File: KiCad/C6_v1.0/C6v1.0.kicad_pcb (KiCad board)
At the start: 2 copper layers, 127 x 127 mm, 0 parts

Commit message: im scared
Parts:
- added 1.8LDO1: LP5907MFX-1.8, Package_TO_SOT_SMD:SOT-23-5, F.Cu at (49.9, 106.4)
- added 2.8LDO1: LP5907MFX-2.8, Package_TO_SOT_SMD:SOT-23-5, F.Cu at (49.9, 111.0)
- added BMS1: BQ29209DRBR, BQ29209:DRB8_1P6X2P4, F.Cu at (112.3, 51.1)
- added BUCKCONV1: TPS563200, Package_TO_SOT_SMD:SOT-23-6, F.Cu at (108.2, 63.5)
- added BatteryConnector1: B03B-XASK-1, B03B-XASK-1_JST:CONN_B03B-XASK-1_JST, F.Cu at (99.8, 47.2)
- added C1: 0.1u, Capacitor_SMD:C_0805_2012Metric, F.Cu at (-11.4, 34.5)
- added C10: 0.1u, Capacitor_SMD:C_0805_2012Metric, F.Cu at (-17.9, 96.6)
- added C11: 0.1u, Capacitor_SMD:C_0805_2012Metric, F.Cu at (-17.9, 99.6)
- added C12: 10u, Capacitor_SMD:C_0805_2012Metric, F.Cu at (-17.9, 102.6)
- added C13: 18p, Capacitor_SMD:C_0805_2012Metric, F.Cu at (-17.9, 105.6)
- added C14: 0.1u, Capacitor_SMD:C_0201_0603Metric_Pad0.64x0.40mm_HandSolder, F.Cu at (-2.70, 110.4)
- added C15: 18p, Capacitor_SMD:C_0805_2012Metric, F.Cu at (-17.9, 108.6)
- added C16: 0.1u, Capacitor_SMD:C_0805_2012Metric, F.Cu at (-17.9, 111.6)
- added C17: 18p, Capacitor_SMD:C_0805_2012Metric, F.Cu at (-17.9, 114.6)
- added C18: 10u, Capacitor_SMD:C_0805_2012Metric, F.Cu at (-13.5, 88.6)
- added C19: 0.1u, Capacitor_SMD:C_0805_2012Metric, F.Cu at (-13.5, 91.6)
- added C2: 1u, Capacitor_SMD:C_0805_2012Metric, F.Cu at (-11.4, 37.5)
- added C20: 0.1uF, Capacitor_SMD:C_1206_3216Metric, F.Cu at (112.0, 46.8)
- added C21: CL10B105KP8NNNC 1uf, Capacitor_SMD:C_1206_3216Metric, F.Cu at (38.9, 97.7)
- added C22: CL10B105KP8NNNC 1uf, Capacitor_SMD:C_1206_3216Metric, F.Cu at (38.9, 101.0)
- added C23: CL10B105KP8NNNC 1uf, Capacitor_SMD:C_1206_3216Metric, F.Cu at (38.9, 104.3)
- added C24: CL10B105KP8NNNC 1uf, Capacitor_SMD:C_1206_3216Metric, F.Cu at (38.9, 107.7)
- added C25: CL10B105KP8NNNC 1uf, Capacitor_SMD:C_1206_3216Metric, F.Cu at (38.9, 111.0)
- added C26: CL10B105KP8NNNC 1uf, Capacitor_SMD:C_1206_3216Metric, F.Cu at (38.9, 114.4)
- added C27: CL31B106KAHNNNE/10uf, CL31B106KAHNNNE:CAPC3216X180N, F.Cu at (108.8, 69.8)
- added C28: CL31B106KAHNNNE/10uf, CL31B106KAHNNNE:CAPC3216X180N, F.Cu at (108.8, 67.2)
- added C29: 08053C104KAT2A/0.1uf, Capacitor_SMD:C_1206_3216Metric, F.Cu at (104.0, 65.8)
- added C30: CL10A226MP8NUNE/22uf, Capacitor_SMD:C_1206_3216Metric, F.Cu at (118.5, 84.5)
- added C31: CL10A226MP8NUNE/22uf, Capacitor_SMD:C_1206_3216Metric, F.Cu at (114.8, 84.5)
- added C32: 2.2u, Capacitor_SMD:C_0805_2012Metric, F.Cu at (-11.4, 52.5)
- added C33: 2.2u, Capacitor_SMD:C_0805_2012Metric, F.Cu at (-11.4, 55.5)
- added C34: 0.1uF, Capacitor_SMD:C_1206_3216Metric, F.Cu at (106.2, 45.5)
- added C35: 10uF, Capacitor_SMD:C_1206_3216Metric, F.Cu at (95.0, 59.2)
- added C36: 0.33uF, Capacitor_SMD:C_1206_3216Metric, F.Cu at (106.2, 54.5)
- added C37: 0.1uF, Capacitor_SMD:C_1206_3216Metric, F.Cu at (95.0, 56.2)
- added C38: 0.1uF, Capacitor_SMD:C_1206_3216Metric, F.Cu at (110.5, 55.8)
- added C39: 0.1uF, Capacitor_SMD:C_1206_3216Metric, F.Cu at (126.0, 51.8)
- added C4: 0.1u, Capacitor_SMD:C_0805_2012Metric, F.Cu at (-11.4, 40.5)
- added C40: 0.1uF, Capacitor_SMD:C_1206_3216Metric, F.Cu at (119.8, 54.0)
- added C41: 0.1u, Capacitor_SMD:C_1206_3216Metric, F.Cu at (48.5, 39.2)
- added C5: 10u, Capacitor_SMD:C_0805_2012Metric, F.Cu at (-11.4, 43.5)
- added C6: 0.1u, Capacitor_SMD:C_0805_2012Metric, F.Cu at (-11.4, 46.5)
- added C7: 0.1u, Capacitor_SMD:C_0805_2012Metric, F.Cu at (29.0, 100.5)
- added C8: 0.1u, Capacitor_SMD:C_0805_2012Metric, F.Cu at (29.0, 103.5)
- added C9: 10p, Capacitor_SMD:C_0805_2012Metric, F.Cu at (-11.4, 49.5)
- added Current_Monitor1: INA219AxD, Package_SO:SOIC-8_3.9x4.9mm_P1.27mm, F.Cu at (101.5, 60.0)
- added DSUB1: ICD15S13E4GX00LF, ICD15S13E4GX00LF:AMPHENOL_ICD15S13E4GX00LF, F.Cu at (117.4, 39.5)
- added FB2: FerriteBead, Resistor_SMD:R_0805_2012Metric, F.Cu at (-7.00, 51.7)
- added FB3: FerriteBead, Inductor_SMD:L_0201_0603Metric_Pad0.64x0.40mm_HandSolder, F.Cu at (-2.70, 112.2)
- added H1: MountingHole, MountingHole:MountingHole_2.2mm_M2_Pad, F.Cu at (-25.1, 74.0)
- added H2: MountingHole, MountingHole:MountingHole_2.2mm_M2_Pad, F.Cu at (-25.1, 79.9)
- added H3: MountingHole, MountingHole:MountingHole_2.2mm_M2_Pad, F.Cu at (-25.1, 85.9)
- added H4: MountingHole, MountingHole:MountingHole_2.2mm_M2_Pad, F.Cu at (-25.1, 91.8)
- added J1: Conn_01x06_Pin, Connector_PinHeader_2.54mm:PinHeader_1x06_P2.54mm_Vertical, F.Cu at (-6.91, 35.3)
- added J2: Conn_01x06_Pin, Connector_PinHeader_2.54mm:PinHeader_1x06_P2.54mm_Vertical, F.Cu at (-2.32, 35.3)
- added J3: Conn_01x06, Connector_JST:JST_XA_B06B-XASK-1_1x06_P2.50mm_Vertical, F.Cu at (14.0, 74.2)
- added J4: 472192001, Connector_Card:microSD_HC_Molex_47219-2001, F.Cu at (-7.37, 79.0)
- added J5: Conn_01x05_Socket, Connector_PinSocket_2.00mm:PinSocket_1x05_P2.00mm_Vertical, F.Cu at (41.0, 74.2)
- added J6: Conn_01x06, Connector_JST:JST_XA_B06B-XASK-1_1x06_P2.50mm_Vertical, F.Cu at (37.0, 57.5)
- added J7: FH12-24S-0.5SH_55_, C6:CONN_FH12-22S-0.5SH55_HIR, F.Cu at (21.0, 93.0)
- added J8: Conn_01x02, Connector_PinHeader_2.54mm:PinHeader_1x02_P2.54mm_Vertical, F.Cu at (-25.8, 64.2)
- added J9: Conn_01x02, Connector_PinHeader_2.54mm:PinHeader_1x02_P2.54mm_Vertical, F.Cu at (-21.2, 64.2)
- added L1: SRN8040-3R3Y/3.3uH, Inductor_SMD:L_Bourns-SRN8040_8x8.15mm, F.Cu at (116.2, 76.5)
- added LED1: LTST-C190KRKT, LTST_C190KRKT:LED_LTST-C190_LTO, F.Cu at (103.0, 72.9)
- added LED2: LTST-C190KRKT, LTST_C190KRKT:LED_LTST-C190_LTO, F.Cu at (53.7, 97.2)
- added LED3: LTST-C190KRKT, LTST_C190KRKT:LED_LTST-C190_LTO, F.Cu at (53.7, 99.7)
- added LED4: LTST-C190KRKT, LTST_C190KRKT:LED_LTST-C190_LTO, F.Cu at (53.7, 102.2)
- added Q1: 2N2219, Package_TO_SOT_THT:TO-39-3, F.Cu at (117.4, 61.5)
- added Q2: NTR4501NT1G, NTR4501NT1G:SOT95P237X111-3N, F.Cu at (126.4, 56.4)
- added Q3: PMOS, NTR4501NT1G:SOT95P237X111-3N, F.Cu at (119.1, 49.2)
- added R1: R22, Resistor_SMD:R_0805_2012Metric, F.Cu at (29.0, 106.5)
- added R10: R22, Resistor_SMD:R_0805_2012Metric, F.Cu at (-7.00, 60.6)
- added R11: R22, Resistor_SMD:R_0805_2012Metric, F.Cu at (-7.00, 63.5)
- added R12: R22, Resistor_SMD:R_0805_2012Metric, F.Cu at (-2.59, 51.7)
- added R13: R22, Resistor_SMD:R_0805_2012Metric, F.Cu at (-2.59, 54.7)
- added R14: R22, Resistor_SMD:R_0805_2012Metric, F.Cu at (-2.59, 57.6)
- added R15: R22, Resistor_SMD:R_0805_2012Metric, F.Cu at (-2.59, 60.6)
- added R16: R22, Resistor_SMD:R_0805_2012Metric, F.Cu at (-2.59, 63.5)
- added R17: YC164-JR-0733RL, C6:RES_YC124_2X1_YAG-L, F.Cu at (-9.76, 113.6)
- added R18: YC164-JR-0733RL, C6:RES_YC124_2X1_YAG-L, F.Cu at (-6.71, 113.6)
- added R19: R33, Resistor_SMD:R_0402_1005Metric_Pad0.72x0.64mm_HandSolder, F.Cu at (0.34, 110.5)
- added R2: R22, Resistor_SMD:R_0805_2012Metric, F.Cu at (29.0, 109.5)
- added R20: R0, Resistor_SMD:R_0805_2012Metric, F.Cu at (-13.5, 105.8)
- added R21: R51, Resistor_SMD:R_0805_2012Metric, F.Cu at (-13.5, 108.8)
- added R22: 10k, Resistor_SMD:R_0805_2012Metric, F.Cu at (-13.5, 111.8)
- added R23: 10k, Resistor_SMD:R_0805_2012Metric, F.Cu at (1.82, 51.7)
- added R24: 10k, Resistor_SMD:R_0805_2012Metric, F.Cu at (1.82, 54.7)
- added R25: 10k, Resistor_SMD:R_0805_2012Metric, F.Cu at (-17.9, 72.5)
- added R26: 10k, Resistor_SMD:R_0805_2012Metric, F.Cu at (-17.9, 75.4)
- added R27: 10k, Resistor_SMD:R_0805_2012Metric, F.Cu at (-17.9, 78.4)
- added R28: 10k, Resistor_SMD:R_0805_2012Metric, F.Cu at (-17.9, 81.3)
- added R29: 10k, Resistor_SMD:R_0805_2012Metric, F.Cu at (-17.9, 84.3)
- added R3: 200k, Resistor_SMD:R_0805_2012Metric, F.Cu at (12.6, 100.5)
- added R30: R22, Resistor_SMD:R_0805_2012Metric, F.Cu at (-17.9, 87.2)
- added R31: 68k 1%, Resistor_SMD:R_0603_1608Metric_Pad0.98x0.95mm_HandSolder, F.Cu at (60.0, 36.2)
- added R32: 33k 1%, Resistor_SMD:R_0603_1608Metric_Pad0.98x0.95mm_HandSolder, F.Cu at (60.0, 38.2)
- added R33: 51k, Resistor_SMD:R_1206_3216Metric, F.Cu at (116.8, 54.0)
- added R34: 160, Resistor_SMD:R_1206_3216Metric, F.Cu at (116.0, 48.5)
- added R35: 260, Resistor_SMD:R_1206_3216Metric, F.Cu at (106.2, 48.5)
- added R36: 100, Resistor_SMD:R_1206_3216Metric, F.Cu at (106.2, 51.5)
- added R37: 2m, Resistor_SMD:R_1206_3216Metric, F.Cu at (107.5, 58.5)
- added R38: 330k, Resistor_SMD:R_1206_3216Metric, F.Cu at (122.8, 49.0)
- added R39: 100, Resistor_SMD:R_1206_3216Metric, F.Cu at (113.6, 55.7)
- added R4: 2.2k, Resistor_SMD:R_0805_2012Metric, F.Cu at (12.6, 103.4)
- added R40: 1k, Resistor_SMD:R_1206_3216Metric, F.Cu at (130.0, 56.0)
- added R41: 470k, Resistor_SMD:R_1206_3216Metric, F.Cu at (122.8, 54.0)
- added R42: RC0805FR-07150RL, Resistor_SMD:R_1206_3216Metric, F.Cu at (44.5, 105.7)
- added R43: ERJ-2RKF1000X, Resistor_SMD:R_1206_3216Metric, F.Cu at (44.5, 109.0)
- added R44: RC0805FR-07150RL, Resistor_SMD:R_1206_3216Metric, F.Cu at (44.5, 112.3)
- added R45: 10k, Resistor_SMD:R_1206_3216Metric, F.Cu at (95.0, 62.0)
- added R46: RC1206FR-07249RL/220ohm, Resistor_SMD:R_1206_3216Metric, F.Cu at (101.5, 77.2)
- added R47: RC0201FR-0756K2L/56.2K ohm, Resistor_SMD:R_1206_3216Metric, F.Cu at (104.5, 77.2)
- added R48: RC0201FR-0710KL/10kohm, Resistor_SMD:R_1206_3216Metric, F.Cu at (108.8, 72.7)
- added R49: 10k, Resistor_SMD:R_0805_2012Metric, F.Cu at (1.82, 57.6)
- added R5: 2.2k, Resistor_SMD:R_0805_2012Metric, F.Cu at (12.6, 106.4)
- added R50: 10k, Resistor_SMD:R_0805_2012Metric, F.Cu at (1.82, 60.6)
- added R6: 2.2k, Resistor_SMD:R_0805_2012Metric, F.Cu at (12.6, 109.3)
- added R7: 2.2k, Resistor_SMD:R_0805_2012Metric, F.Cu at (12.6, 112.3)
- added R8: 220, Resistor_SMD:R_0805_2012Metric, F.Cu at (-7.00, 55.0)
- added R9: 220, Resistor_SMD:R_0805_2012Metric, F.Cu at (-7.00, 57.6)
- added SW1: SLW-1277545-3A-RA-N-D, SLW_1277545_3A_RA_N_D:SW_SLW-1277545-3A-RA-N-D, F.Cu at (97.0, 70.8)
- added U1: STM32H562RITx, Package_QFP:LQFP-64_10x10mm_P0.5mm, F.Cu at (-20.9, 40.2)
- added U10: REF35330QDBVR, Package_TO_SOT_SMD:SOT-23-6, F.Cu at (2.55, 41.9)
- added U2: STM32H7A3RITx, Package_QFP:LQFP-64_10x10mm_P0.5mm, F.Cu at (-20.9, 54.6)
- added U3: PCA9306, Package_SON:X2SON-8_1.4x1mm_P0.35mm, F.Cu at (16.3, 100.5)
- added U4: SN74CB3T3384PWR, C6:PW24-L, F.Cu at (-11.2, 99.7)
- added U5: SN74CB3T3384PWR, C6:PW24-L, F.Cu at (0.75, 94.8)
- added U6: ADV7280AWBCPZ, C6:CP-32-12_ADI-L, F.Cu at (-7.86, 108.1)
- added U7: MAX3490xSA, Package_SO:SOIC-8_3.9x4.9mm_P1.27mm, F.Cu at (4.20, 36.3)
- added U8: TLV1117LV33DCYR, TLV1117LV33DCYR:VREG_TLV1117LV33DCYR, F.Cu at (47.0, 100.0)
- added U9: OPA340NA, Package_TO_SOT_SMD:SOT-23-5, F.Cu at (54.1, 37.5)
- added Y1: SIT5000AICGE-33E0-25.000000X, Oscillator:Oscillator_SMD_SiT_PQFN-4Pin_5.0x3.2mm, F.Cu at (23.2, 101.7)
- added Y2: SIT5000AICGE-33E0-25.000000X, Oscillator:Oscillator_SMD_SiT_PQFN-4Pin_5.0x3.2mm, F.Cu at (23.2, 107.1)
- added Y3: ABM8AIG-28.63636MHZ, C6:XTAL_ABM8AIG-28.63636MHZ-12-2Z-T3, F.Cu at (-1.25, 107.0)
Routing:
- net /5V: track 0.00 -> 34.0 mm, vias 0 -> 3
- net Net-(BUCKCONV1-VFB): track 0.00 -> 26.3 mm, vias 0 -> 3
- net Net-(R45-Pad2): track 0.00 -> 14.2 mm
- net Net-(Q1-C): track 0.00 -> 12.0 mm
- net Net-(BMS1-VC1): track 0.00 -> 10.4 mm
- net Net-(Q1-B): track 0.00 -> 9.92 mm
- net GND: track 0.00 -> 9.78 mm, vias 0 -> 15
- net Net-(BatteryConnector1-Pad2): track 0.00 -> 8.50 mm
- net Net-(BMS1-VDD): track 0.00 -> 7.82 mm
- net Net-(BMS1-VC2): track 0.00 -> 7.41 mm
- net /8V4: track 0.00 -> 6.20 mm
- net /Power/Buck Converter/buck-vbst_cap: track 0.00 -> 5.94 mm, vias 0 -> 10
- net Net-(BUCKCONV1-VBST): track 0.00 -> 4.86 mm
- net /Power/8V4_Evil: track 0.00 -> 4.69 mm, vias 0 -> 15
- net Net-(Q2-Pad3): track 0.00 -> 4.38 mm
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- added copper zone on F.Cu, net +5V
- added copper zone on In2.Cu, net +5V
- added copper zone on F.Cu, net /8V4
- added copper zone on F.Cu, net /Power/8V4_Evil
- added copper zone on In2.Cu, net /Power/8V4_Evil
- added copper zone on F.Cu, net /Power/Buck Converter/buck-vbst_cap
- added copper zone on In2.Cu, net /Power/Buck Converter/buck-vbst_cap
- added copper zone on F.Cu, net /Power/VOUT
- added copper zone on In2.Cu, net /Power/VOUT
- added copper zone on F.Cu, net /Power/bruh
- added copper zone on F.Cu, net GND
- added copper zone on In1.Cu, net GND
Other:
- copper layers 2 -> 4

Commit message: DCMI1-Me0
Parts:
- added J10: Conn_01x03, Connector_JST:JST_XA_S03B-XASK-1_1x03_P2.50mm_Horizontal, F.Cu at (66.5, 85.6)
- added J11: Conn_01x06, Connector_JST:JST_XA_S06B-XASK-1_1x06_P2.50mm_Horizontal, F.Cu at (66.5, 71.0)
- added J12: Conn_02x10_Odd_Even, Connector_PinHeader_2.54mm:PinHeader_2x10_P2.54mm_Vertical, F.Cu at (58.2, 68.8)
- C1, C10, C11, C12, C13, C15, C16, C17, C18, C19, C2, C32, C33, C4, C5, C6, C7, C8, C9: footprint Capacitor_SMD:C_0805_2012Metric -> Capacitor_SMD:C_0402_1005Metric_Pad0.74x0.62mm_HandSolder
- C14: footprint Capacitor_SMD:C_0201_0603Metric_Pad0.64x0.40mm_HandSolder -> Capacitor_SMD:C_0402_1005Metric_Pad0.74x0.62mm_HandSolder
- J3, J6: footprint Connector_JST:JST_XA_B06B-XASK-1_1x06_P2.50mm_Vertical -> Connector_JST:JST_XA_S06B-XASK-1_1x06_P2.50mm_Horizontal
- R1, R10, R11, R12, R13, R14, R15, R16, R2, R20, R21, R22, R23, R24, R25, R26, R27, R28, R29, R3, R30, R4, R49, R5, R50, R6, R7, R8, R9: footprint Resistor_SMD:R_0805_2012Metric -> Resistor_SMD:R_0402_1005Metric_Pad0.72x0.64mm_HandSolder
- moved C12 191.7 mm to (172.4, 80.1), turned to 90 degrees
- moved C13 191.6 mm to (172.4, 83.3)
- moved C15 191.3 mm to (172.3, 88.5), turned to 180 degrees
- moved C16 190.6 mm to (169.6, 77.7), turned to 180 degrees
- moved C17 189.5 mm to (167.8, 76.9), turned to -90 degrees
- moved R21 186.6 mm to (170.2, 76.0), turned to -90 degrees
- moved R20 183.9 mm to (169.3, 85.2), turned to 135 degrees
- moved U4 182.2 mm to (170.9, 105.3)
- moved R22 181.9 mm to (165.1, 76.9), turned to 180 degrees
- moved FB3 180.3 mm to (174.8, 80.8), turned to 180 degrees
- moved U2 179.5 mm to (151.0, 106.4), turned to 135 degrees
- moved C14 176.8 mm to (171.4, 80.1), turned to 90 degrees
- moved U6 175.2 mm to (165.5, 82.5), turned to 45 degrees
- moved Y3 174.9 mm to (172.3, 85.9), turned to 180 degrees
- moved J7 167.0 mm to (187.3, 108.3), turned to 90 degrees
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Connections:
- net /STM32/PPS renamed /PPS
- R45 pad 2: Net-(R45-Pad2) -> Net-(BUCKCONV1-EN)
- U1 pad 20: unconnected-(U1-PA4-Pad20) -> /HALL_C
- U1 pad 22: unconnected-(U1-PA6-Pad22) -> /HALL_B
- U1 pad 23: unconnected-(U1-PA7-Pad23) -> /HALL_A
- U1 pad 27: unconnected-(U1-PB1-Pad27) -> /ESC_PWM
- U1 pad 57: unconnected-(U1-PB5-Pad57) -> /ESC_TLM
- U4 pad 10: /CAM_D4 -> unconnected-(U4-1B5-Pad10)
- U4 pad 11: /OV_D4 -> GND
- U4 pad 14: /OV_D5 -> /OV_D7
- U4 pad 15: /CAM_D5 -> /CAM_D7
- U4 pad 18: /OV_D7 -> /OV_PCLK
- U4 pad 19: /CAM_D7 -> /CAM_PCLK
- U4 pad 2: /CAM_D0 -> /CAM_D2
- U4 pad 20: /CAM_PCLK -> /CAM_D0
- U4 pad 21: /OV_PCLK -> /OV_D0
- U4 pad 22: GND -> /OV_D1
- U4 pad 23: unconnected-(U4-2B5-Pad23) -> /CAM_D1
- U4 pad 3: /OV_D0 -> /OV_D2
- U4 pad 4: /OV_D1 -> /OV_D3
- U4 pad 5: /CAM_D1 -> /CAM_D3
- U4 pad 6: /CAM_D2 -> /CAM_D4
- U4 pad 7: /OV_D2 -> /OV_D4
- U4 pad 8: /OV_D3 -> /OV_D5
- U4 pad 9: /CAM_D3 -> /CAM_D5
- U6 pad 21: /1V8 -> /CameraManagement/1V8*
- U7 pad 5: /STM32/RX- -> /RS422_RX-
- U7 pad 6: /STM32/RX+ -> /RS422_RX+
- U7 pad 7: /STM32/TX- -> /RS422_TX-
- U7 pad 8: /STM32/TX+ -> /RS422_TX+
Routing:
- net /CameraManagement/1V8*: track 0.00 -> 30.8 mm, vias 0 -> 5
- net /OV_D7: track 0.00 -> 19.5 mm
- net /OV_D0: track 0.00 -> 19.4 mm
- net /OV_D6: track 0.00 -> 19.4 mm
- net /OV_PCLK: track 0.00 -> 19.4 mm
- net /OV_D1: track 0.00 -> 19.4 mm
- net /OV_D4: track 0.00 -> 16.5 mm, vias 0 -> 2
- net /OV_D2: track 0.00 -> 16.5 mm, vias 0 -> 2
- net /OV_D3: track 0.00 -> 16.4 mm, vias 0 -> 2
- net /OV_D5: track 0.00 -> 16.4 mm, vias 0 -> 2
- net /CameraManagement/SPLIT_PCLK: track 0.00 -> 16.3 mm
- net /NTSC: track 0.00 -> 14.8 mm
- net /CameraManagement/SPLIT_D7: track 0.00 -> 14.3 mm
- net /CameraManagement/SPLIT_D0: track 0.00 -> 12.5 mm
- net /CameraManagement/SPLIT_D6: track 0.00 -> 12.2 mm
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
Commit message: john d tickle
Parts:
- removed SW1: SLW-1277545-3A-RA-N-D, SLW_1277545_3A_RA_N_D:SW_SLW-1277545-3A-RA-N-D
- moved BatteryConnector1 14.9 mm to (103.5, 32.8), turned to 0 degrees
- moved C40 13.0 mm to (132.8, 54.5)
- moved DSUB1 13.0 mm to (130.4, 40.0)
- moved Q1 13.0 mm to (130.4, 62.0)
- moved R33 13.0 mm to (129.8, 54.5)
- moved R39 13.0 mm to (126.6, 56.1)
- moved BMS1 13.0 mm to (125.3, 51.6)
- moved BUCKCONV1 13.0 mm to (121.2, 64.0)
- moved C20 13.0 mm to (125.0, 47.2)
- moved C27 13.0 mm to (121.7, 70.2)
- moved C28 13.0 mm to (121.7, 67.7)
- moved C29 13.0 mm to (117.0, 66.3)
- moved C30 13.0 mm to (131.5, 85.0)
- moved C31 13.0 mm to (127.7, 85.0)
- moved C34 13.0 mm to (119.2, 46.0)
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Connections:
- DSUB1 pad S1: unconnected-(DSUB1-SHIELD-PadS1) -> GND
- DSUB1 pad S2: unconnected-(DSUB1-SHIELD__1-PadS2) -> GND
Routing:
- net Net-(R45-Pad2): track 14.2 -> 0.00 mm
- net GND: vias 15 -> 17

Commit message: sneaky commit
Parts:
- removed BatteryConnector1: B03B-XASK-1, B03B-XASK-1_JST:CONN_B03B-XASK-1_JST
- added J13: S02B-XASS-1LFSN, idk:CONN2_S02B-XASS_295x496_JST, F.Cu at (190.0, 40.0)
- added J14: Conn_01x03, Connector_JST:JST_XA_S03B-XASK-1_1x03_P2.50mm_Horizontal, F.Cu at (107.5, 42.9)
- moved J3 139.3 mm to (136.2, 141.0)
- moved J12 43.4 mm to (100.1, 80.2)
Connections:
- R45 pad 1: /8V4 -> Net-(BUCKCONV1-EN)
- R45 pad 2: Net-(BUCKCONV1-EN) -> GND
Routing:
- net Net-(BUCKCONV1-EN): track 0.00 -> 6.20 mm
- net /8V4: track 6.20 -> 0.00 mm

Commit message: finaly
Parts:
- removed C11: 0.1u, Capacitor_SMD:C_0402_1005Metric_Pad0.74x0.62mm_HandSolder
- removed DSUB1: ICD15S13E4GX00LF, ICD15S13E4GX00LF:AMPHENOL_ICD15S13E4GX00LF
- removed J13: S02B-XASS-1LFSN, idk:CONN2_S02B-XASS_295x496_JST
- removed R10, R11, R12, R13: R22, Resistor_SMD:R_0402_1005Metric_Pad0.72x0.64mm_HandSolder
- removed R19: R33, Resistor_SMD:R_0402_1005Metric_Pad0.72x0.64mm_HandSolder
- removed R23: 10k, Resistor_SMD:R_0402_1005Metric_Pad0.72x0.64mm_HandSolder
- removed R45: 10k, Resistor_SMD:R_1206_3216Metric
- removed U4, U5: SN74CB3T3384PWR, C6:PW24-L
- added C3: 2.2u, Capacitor_SMD:C_0402_1005Metric_Pad0.74x0.62mm_HandSolder, F.Cu at (114.2, 108.7)
- added J15: Conn_02x03_Odd_Even, C6:CONN_SD-44764-001_06_MOL, F.Cu at (195.6, 33.2)
- added R51: R33, Resistor_SMD:R_0402_1005Metric_Pad0.72x0.64mm_HandSolder, B.Cu at (180.9, 103.0)
- added R52: R33, Resistor_SMD:R_0402_1005Metric_Pad0.72x0.64mm_HandSolder, B.Cu at (180.9, 102.0)
- added R53: R33, Resistor_SMD:R_0402_1005Metric_Pad0.72x0.64mm_HandSolder, B.Cu at (180.9, 101.0)
- added R54: R33, Resistor_SMD:R_0402_1005Metric_Pad0.72x0.64mm_HandSolder, B.Cu at (180.9, 99.9)
- added R55: R33, Resistor_SMD:R_0402_1005Metric_Pad0.72x0.64mm_HandSolder, B.Cu at (180.9, 98.9)
- added R56: R33, Resistor_SMD:R_0402_1005Metric_Pad0.72x0.64mm_HandSolder, B.Cu at (180.9, 97.9)
- added R57: R33, Resistor_SMD:R_0402_1005Metric_Pad0.72x0.64mm_HandSolder, B.Cu at (180.9, 96.9)
- added R58: R33, Resistor_SMD:R_0402_1005Metric_Pad0.72x0.64mm_HandSolder, B.Cu at (180.9, 95.9)
- added R59: R33, Resistor_SMD:R_0402_1005Metric_Pad0.72x0.64mm_HandSolder, B.Cu at (180.9, 94.9)
- added R60: R33, Resistor_SMD:R_0402_1005Metric_Pad0.72x0.64mm_HandSolder, B.Cu at (180.9, 93.9)
- added R61: R33, Resistor_SMD:R_0402_1005Metric_Pad0.72x0.64mm_HandSolder, B.Cu at (180.9, 92.8)
- added R62: YC164-JR-0733RL, C6:RES_YC124_2X1_YAG-L, F.Cu at (146.1, 100.3)
- added U11: SN74CBTLV16292VR, C6:DGV56-L, F.Cu at (151.5, 96.6)
- C10: value 0.1u -> 2.2u
- FB3: footprint Inductor_SMD:L_0201_0603Metric_Pad0.64x0.40mm_HandSolder -> Inductor_SMD:L_0805_2012Metric_Pad1.15x1.40mm_HandSolder
- J7: moved to B.Cu
- U3: footprint Package_SON:X2SON-8_1.4x1mm_P0.35mm -> Package_SO:SSOP-8_2.95x2.8mm_P0.65mm
- moved H4 226.4 mm to (198.1, 129.7)
- moved U1 226.2 mm to (139.7, 121.3), turned to -135 degrees
- moved H3 225.6 mm to (198.1, 53.5)
- moved R25 206.3 mm to (175.0, 145.4)
- moved R27 206.3 mm to (175.0, 151.3)
- moved R26 205.6 mm to (175.0, 146.6)
- moved R28 205.6 mm to (175.0, 152.4)
- moved R29 203.9 mm to (175.0, 150.1)
- moved C18 197.6 mm to (175.0, 147.7)
- moved C19 197.1 mm to (175.0, 149.0)
- moved C9 190.9 mm to (176.3, 84.6), turned to -90 degrees
- moved J9 185.7 mm to (153.7, 126.5), turned to -90 degrees
- moved R9 185.6 mm to (176.9, 82.9)
- moved J4 185.3 mm to (164.7, 147.7)
- moved R30 179.1 mm to (154.9, 134.1), turned to 135 degrees
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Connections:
- net /DCMI_RST renamed /OV_RST
- net /OV_OE renamed /CAM_S
- 1.8LDO1 pad 1: +2.8V -> /2V8
- 1.8LDO1 pad 3: +2.8V -> /2V8
- 1.8LDO1 pad 5: 1.8V -> /1V8
- 2.8LDO1 pad 1: +3.3V -> /3V3
- 2.8LDO1 pad 3: +3.3V -> /3V3
- 2.8LDO1 pad 5: +2.8V -> /2V8
- BMS1 pad 9: unconnected-(BMS1-EPAD-Pad9) -> GND
- BUCKCONV1 pad 5: Net-(BUCKCONV1-EN) -> /8V4
- C10 pad 1: /3V3 -> Net-(C10-Pad1)
- C21 pad 2: +5V -> /5V
- C22 pad 2: +3.3V -> /3V3
- C23 pad 2: +2.8V -> /2V8
- C24 pad 2: 1.8V -> /1V8
- C25 pad 2: +2.8V -> /2V8
- C26 pad 2: +3.3V -> /3V3
- C30 pad 2: +5V -> /5V
- C31 pad 2: +5V -> /5V
- J11 pad 6: /IO_Connections/3V3 -> /3V3
- J12 pad 3: /IO_Connections/3V3 -> /3V3
- J12 pad 4: /IO_Connections/3V3 -> /3V3
- J7 pad 12: /OV_D7 -> /IO_Connections/D7
- J7 pad 14: /OV_D6 -> /IO_Connections/D6
- J7 pad 16: /OV_D5 -> /IO_Connections/D5
- J7 pad 17: /OV_PCLK -> /IO_Connections/PCLK
- J7 pad 18: /OV_D4 -> /IO_Connections/D4
- J7 pad 19: /OV_D0 -> /IO_Connections/D0
- J7 pad 20: /OV_D3 -> /IO_Connections/D3
- J7 pad 21: /OV_D1 -> /IO_Connections/D1
- J7 pad 22: /OV_D2 -> /IO_Connections/D2
- J7 pad 7: /CAM_VSYNC -> /IO_Connections/VSYNC
- J7 pad 8: /DCMI_PWDN -> /OV_PWDN
- J7 pad 9: /CAM_HSYNC -> /IO_Connections/HSYNC
- L1 pad 1: +5V -> /5V
- R17 pad 1: /CAM_D0 -> /CAM_PWDN*
- R17 pad 2: /CAM_D1 -> /CAM_D7*
- R17 pad 3: /CAM_D2 -> /CAM_D6*
- R17 pad 4: /CAM_D3 -> /CAM_VSYNC*
- R17 pad 5: /CAM_D3 -> /CameraManagement/CAM_VSYNC
- R17 pad 6: /CAM_D2 -> /CameraManagement/CAM_D6
- R17 pad 7: /CAM_D1 -> /CameraManagement/CAM_D7
- R17 pad 8: /CAM_D0 -> /CameraManagement/CAM_PDWN
- R18 pad 1: /CAM_D4 -> /CAM_D5*
- R18 pad 2: /CAM_D5 -> /CAM_D4*
- R18 pad 3: /CAM_D6 -> /CAM_HSYNC*
- R18 pad 4: /CAM_D7 -> /CAM_PCLK*
- R18 pad 5: /CAM_D7 -> /CameraManagement/CAM_PCLK
- R18 pad 6: /CAM_D6 -> /CameraManagement/CAM_HSYNC
- R18 pad 7: /CAM_D5 -> /CameraManagement/CAM_D4
- R18 pad 8: /CAM_D4 -> /CameraManagement/CAM_D5
- R42 pad 1: +2.8V -> /2V8
- R43 pad 1: 1.8V -> /1V8
- R44 pad 1: +3.3V -> /3V3
- R46 pad 2: +5V -> /5V
- R47 pad 2: +5V -> /5V
- U1 pad 29: /STM32/SPI_SCK* -> /STM32/SPI_SCK
- U1 pad 30: Net-(C32-Pad1) -> Net-(C10-Pad1)
- U1 pad 33: /STM32/SPI_NSS* -> /STM32/SPI_NSS
- U1 pad 35: /STM32/SPI_MISO* -> /STM32/SPI_MISO
- U1 pad 36: /STM32/SPI_MOSI* -> /STM32/SPI_MOSI
- U2 pad 10: /SPLIT_OE -> unconnected-(U2-PC2-Pad10)
- U2 pad 20: /CAM_HSYNC -> /CAM_HSYNC*
- U2 pad 22: /CAM_PCLK -> /CAM_PCLK*
- U2 pad 27: /DCD_PWDN -> unconnected-(U2-PB1-Pad27)
- U2 pad 3: /DCMI_PWDN -> /CAM_PWDN*
- U2 pad 30: Net-(C33-Pad1) -> Net-(C3-Pad1)
- U2 pad 34: /CAM_D2 -> /CAM_D2*
- U2 pad 37: /CAM_D0 -> /CAM_D0*
- U2 pad 38: /CAM_D1 -> /CAM_D1*
- U2 pad 39: /CAM_D3 -> /CAM_D3*
- U2 pad 52: /CAM_D4 -> /CAM_D4*
- U2 pad 58: /CAM_D5 -> /CAM_D5*
- U2 pad 59: /CAM_VSYNC -> /CAM_VSYNC*
- U2 pad 61: /CAM_D6 -> /CAM_D6*
- U2 pad 62: /CAM_D7 -> /CAM_D7*
- U6 pad 29: unconnected-(U6-VS/FIELD/SFL-Pad29) -> /CameraManagement/DCD_VSYNC
- U6 pad 30: unconnected-(U6-HS-Pad30) -> /CameraManagement/DCD_HSYNC
- U6 pad 31: /DCD_PDWN -> /CameraManagement/DCD_PWDN
- U8 pad 2: +3.3V -> /3V3
- U8 pad 3: +5V -> /5V
- U8 pad 4: +3.3V -> /3V3
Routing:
- net /I_SDA: track 0.00 -> 247.6 mm, vias 0 -> 2
- net /I_SCL: track 0.00 -> 236.0 mm, vias 0 -> 2
- net /3V3: track 0.00 -> 174.8 mm, vias 0 -> 21
- net /8V4: track 0.00 -> 126.8 mm, vias 0 -> 5
- net /EGSE_RX: track 0.00 -> 126.5 mm, vias 0 -> 2
- net GND: track 13.5 -> 139.9 mm, vias 17 -> 98
- net /EGSE_TX: track 0.00 -> 122.1 mm, vias 0 -> 1
- net /CAM_SDA: track 0.00 -> 120.1 mm, vias 0 -> 4
- net /CAM_SCL: track 0.00 -> 117.8 mm, vias 0 -> 4
- net /SPLIT_TX: track 0.00 -> 100.7 mm, vias 0 -> 1
- net /5V: track 34.0 -> 133.1 mm, vias 3 -> 19
- net /STM32/CAM_RX*: track 0.00 -> 91.2 mm, vias 0 -> 2
- net /OV_RST: track 0.00 -> 76.9 mm, vias 0 -> 5
- net Net-(J14-Pin_2): track 8.50 -> 84.4 mm, vias 0 -> 1
- net /STM32/H7_NRST: track 0.00 -> 74.9 mm, vias 0 -> 2
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- added copper zone on F.Cu, net /1V8
- added copper zone on F.Cu, net /2V8
- added copper zone on In2.Cu, net /2V8
- added copper zone on F.Cu, net /3V3
- added copper zone on In2.Cu, net /3V3
- added copper zone on F.Cu, net /5V
- added copper zone on In2.Cu, net /5V
- added copper zone on In2.Cu, net /8V4
- added copper zone on B.Cu, net GND
- added copper zone on In2.Cu, net GND
- removed copper zone on F.Cu, net +5V
- removed copper zone on In2.Cu, net +5V
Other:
- board text added: "BOOT0"
- board text added: "H5 SWD"
- board text added: "H7 SWD"

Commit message: ewo
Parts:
- FB3: footprint Inductor_SMD:L_0805_2012Metric_Pad1.15x1.40mm_HandSolder -> Inductor_SMD:L_0201_0603Metric_Pad0.64x0.40mm_HandSolder
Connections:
- J15 pad 2: /Power/VOUT -> GND
- J15 pad 3: GND -> /EGSE_RX
- J15 pad 4: GND -> /Power/VOUT
- J15 pad 5: /EGSE_RX -> GND
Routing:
- net /EGSE_RX: track 126.5 -> 129.0 mm, vias 2 -> 1

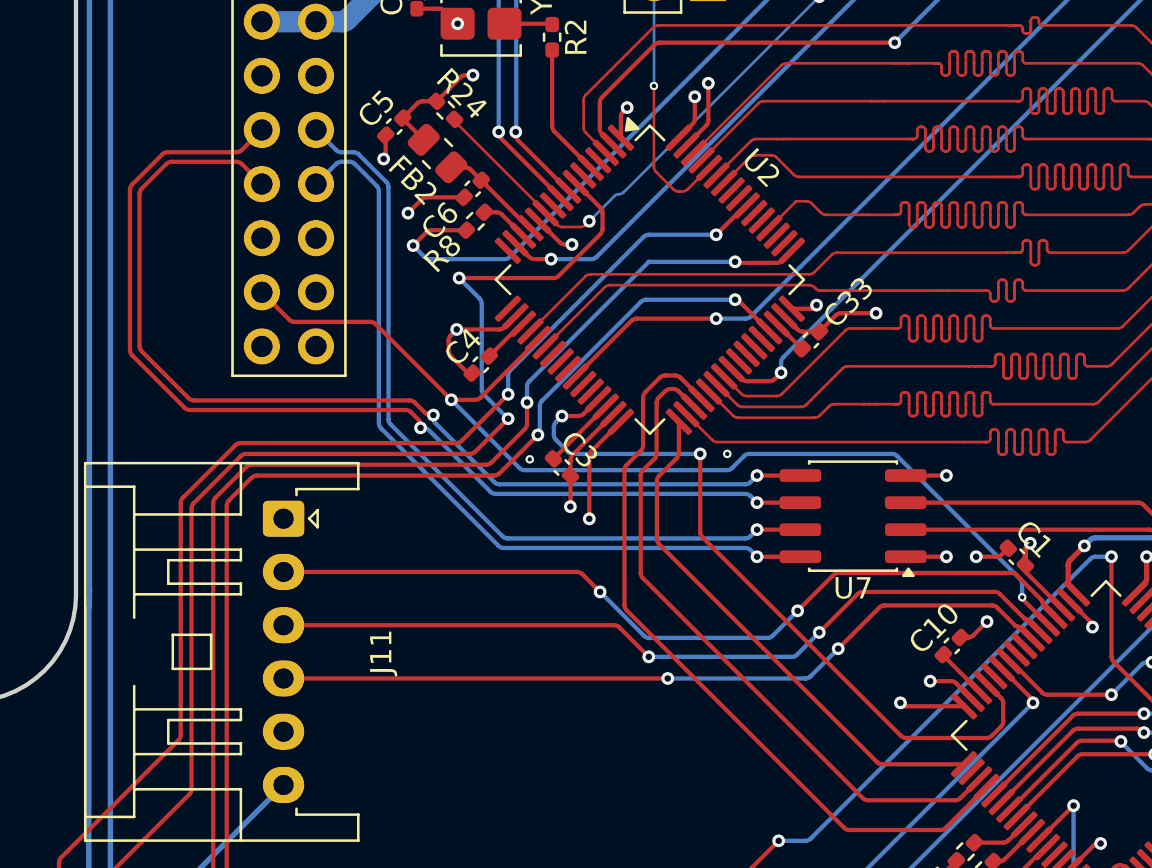
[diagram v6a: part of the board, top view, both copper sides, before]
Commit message: made RS-422 120 impedance
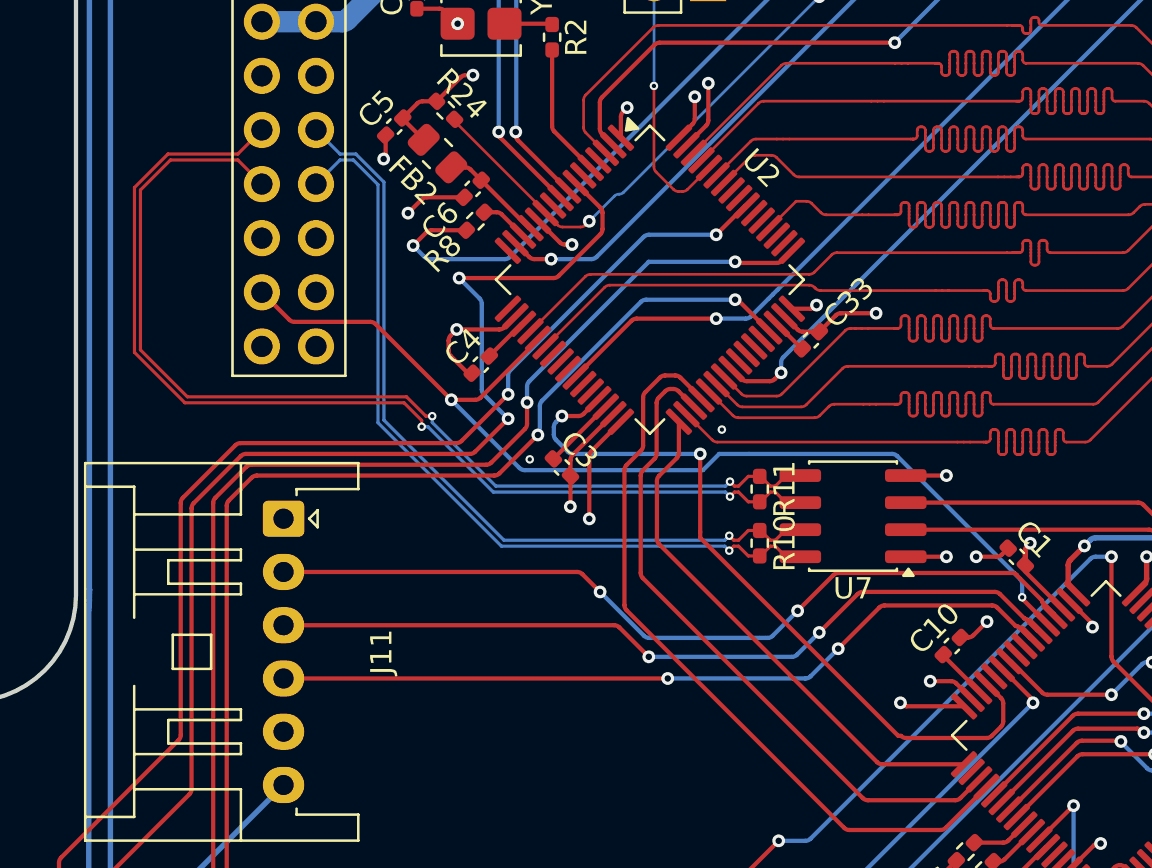
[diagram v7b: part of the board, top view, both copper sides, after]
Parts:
- added R10: 120, Resistor_SMD:R_0402_1005Metric_Pad0.72x0.64mm_HandSolder, F.Cu at (123.4, 112.3)
- added R11: 120, Resistor_SMD:R_0402_1005Metric_Pad0.72x0.64mm_HandSolder, F.Cu at (123.4, 109.7)
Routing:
- net /RS422_RX-: track 48.0 -> 48.8 mm
- net /RS422_TX-: track 37.3 -> 38.0 mm
- net /RS422_TX+: track 37.3 -> 38.0 mm
